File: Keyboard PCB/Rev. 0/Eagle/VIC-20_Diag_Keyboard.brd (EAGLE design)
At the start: 14 x 53 mm, 8 parts, among them J1 BL1-85AXX-20U

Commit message: Add files via upload
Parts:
- added U$10: (no value), Logo:VIC20_DIAG_SMALL
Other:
- board text added: "Keyboard Dongle Rev. 0"
- board text removed: "VIC-20 Diagnostic Keyboard Dongle Rev. 0"
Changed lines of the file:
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@@
 <?xml version="1.0" encoding="utf-8"?>
 <!DOCTYPE eagle SYSTEM "eagle.dtd">
-<eagle version="9.5.2">
+<eagle version="9.6.2">
 <drawing>
 <settings>
@@
 <wire x1="14" y1="0" x2="14" y2="53" width="0" layer="20"/>
 <wire x1="14" y1="53" x2="0" y2="53" width="0" layer="20"/>
-<text x="10.06625" y="39.6825" size="1.27" layer="21" rot="SR270">VIC-20 Diagnostic
-Keyboard Dongle Rev. 0</text>
+<text x="6.415" y="41.905" size="1.27" layer="21" rot="SR270">Keyboard Dongle Rev. 0</text>
 <wire x1="6.19125" y1="5.08" x2="8.5725" y2="5.08" width="0.1524" layer="21"/>
 <wire x1="8.5725" y1="5.08" x2="10.00125" y2="6.50875" width="0.1524" layer="21"/>
@@
 <text x="6.35" y="3.01625" size="1.778" layer="21" ratio="12" rot="SR270">1</text>
 <text x="6.19125" y="51.7525" size="1.778" layer="21" ratio="12" rot="SR270">20</text>
-<text x="8.73125" y="48.73625" size="1.27" layer="21" rot="SR270">!RESTORE</text>
+<text x="8.5725" y="50.4825" size="1.27" layer="21" rot="SR270">!RESTORE</text>
 <hole x="11.90625" y="49.8475" drill="2"/>
 <text x="1.905" y="44.29125" size="1.27" layer="22" rot="MR270">http://github.com/svenpetersen1965</text>
@@
 </element>
 <element name="U$8" library="Logo" package="SVEN_TAG" value="" x="9.525" y="39.52875" smashed="yes" rot="MR0"/>
+<element name="U$10" library="Logo" package="VIC20_DIAG_SMALL" value="" x="8.89" y="41.91" smashed="yes" rot="R270"/>
 </elements>
 <signals>

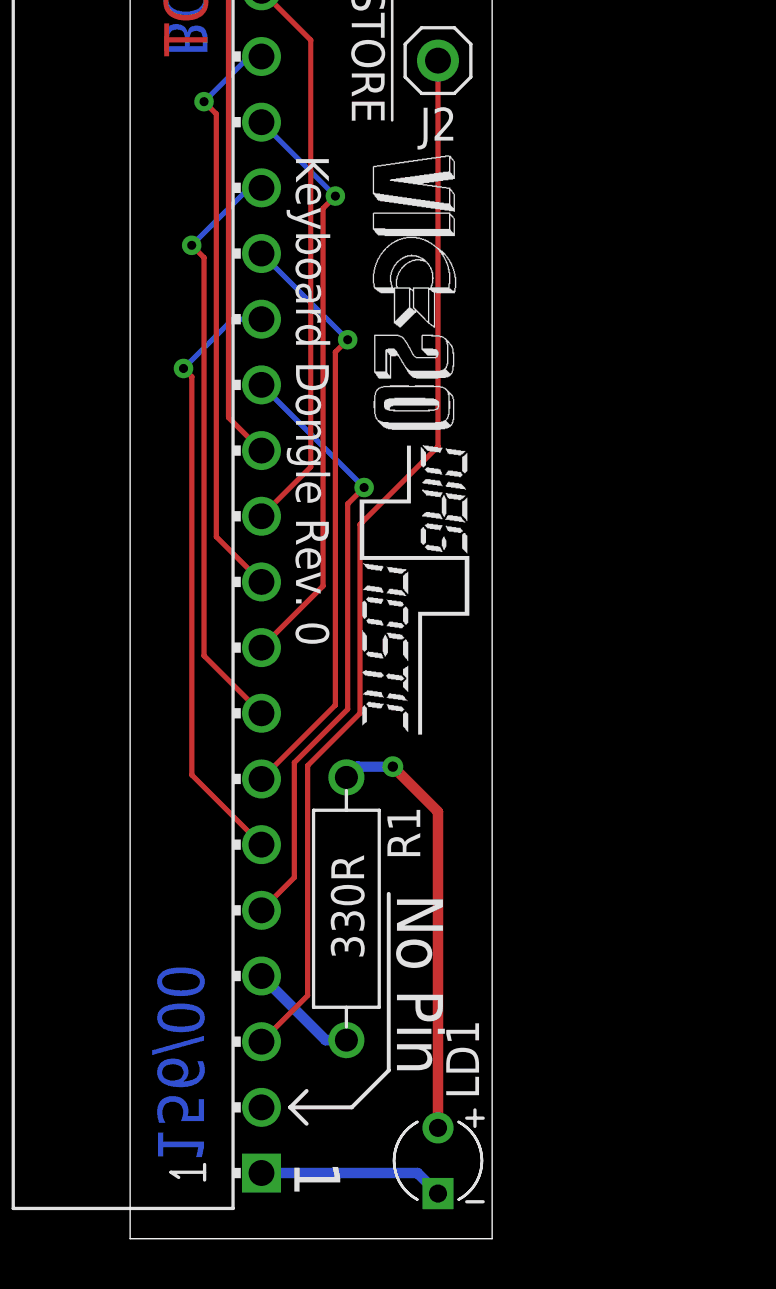
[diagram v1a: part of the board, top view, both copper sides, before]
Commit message: Silk Screen Update
Just a new logo
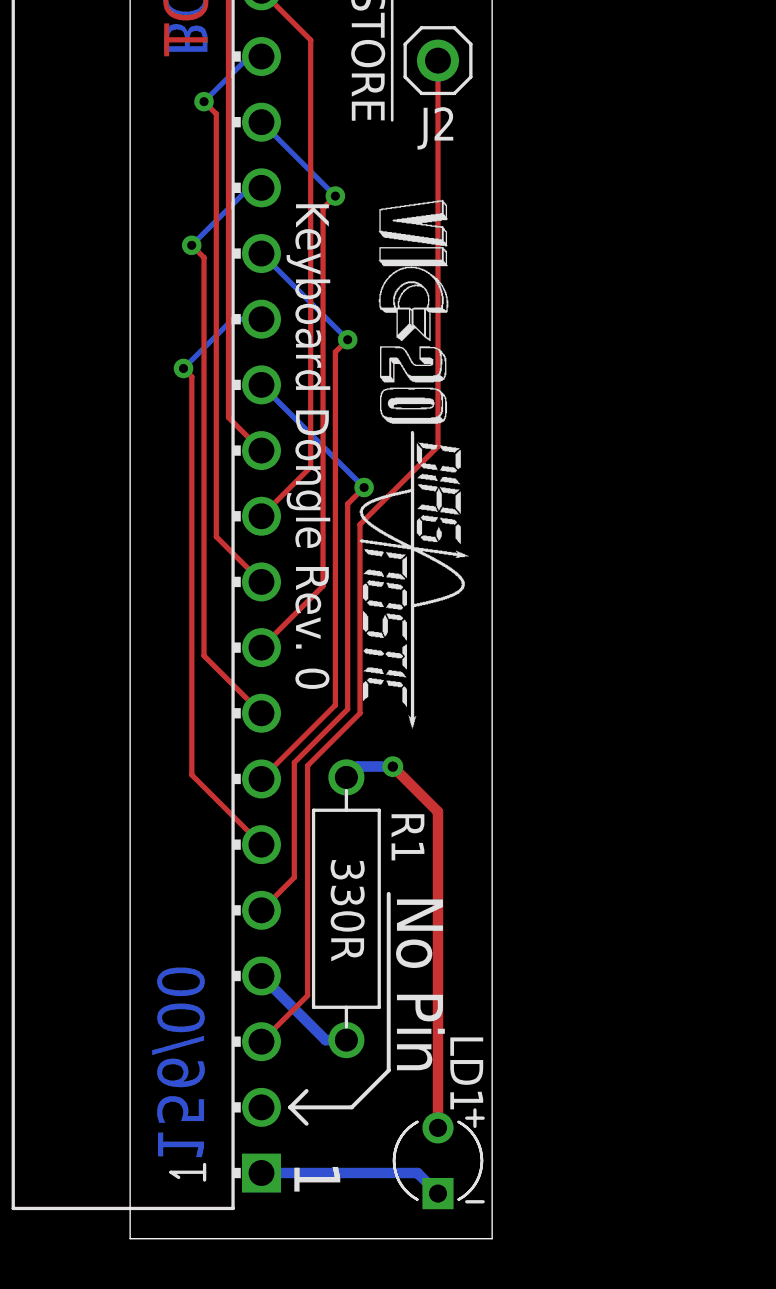
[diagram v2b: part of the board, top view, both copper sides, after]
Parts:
- moved U$10 1.75 mm to (8.89, 40.2)
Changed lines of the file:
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@@
 <layer number="45" name="Holes" color="7" fill="1" visible="no" active="yes"/>
 <layer number="46" name="Milling" color="3" fill="1" visible="no" active="yes"/>
-<layer number="47" name="Measures" color="7" fill="1" visible="no" active="yes"/>
+<layer number="47" name="Measures" color="7" fill="1" visible="yes" active="yes"/>
 <layer number="48" name="Document" color="5" fill="1" visible="yes" active="yes"/>
 <layer number="49" name="Reference" color="7" fill="1" visible="yes" active="yes"/>
@@
 <wire x1="14" y1="0" x2="14" y2="53" width="0" layer="20"/>
 <wire x1="14" y1="53" x2="0" y2="53" width="0" layer="20"/>
-<text x="6.415" y="41.905" size="1.27" layer="21" rot="SR270">Keyboard Dongle Rev. 0</text>
+<text x="6.415" y="40.15875" size="1.27" layer="21" rot="SR270">Keyboard Dongle Rev. 0</text>
 <wire x1="6.19125" y1="5.08" x2="8.5725" y2="5.08" width="0.1524" layer="21"/>
 <wire x1="8.5725" y1="5.08" x2="10.00125" y2="6.50875" width="0.1524" layer="21"/>
@@
 <hole x="11.90625" y="49.8475" drill="2"/>
 <text x="1.905" y="44.29125" size="1.27" layer="22" rot="MR270">http://github.com/svenpetersen1965</text>
-<text x="9.04875" y="10.795" size="1.27" layer="21" rot="R90">330R</text>
+<text x="7.77875" y="14.76375" size="1.27" layer="21" rot="SR270">330R</text>
 </plain>
 <attributes>
@@
 </element>
 <element name="LD1" library="LED" package="3MM" value="" x="11.90625" y="3.01625" smashed="yes" rot="R270">
-<attribute name="NAME" x="13.49375" y="5.3975" size="1.27" layer="25" ratio="10" rot="R90"/>
+<attribute name="NAME" x="12.3825" y="7.9375" size="1.27" layer="25" ratio="10" rot="SR270"/>
 <attribute name="VALUE" x="10.31875" y="1.11125" size="1.27" layer="27" ratio="10" rot="R270"/>
 </element>
 <element name="R1" library="DISCRETE" package="R-10" value="330R" x="8.36375" y="12.76" smashed="yes" rot="R270">
-<attribute name="NAME" x="9.95125" y="16.72875" size="1.27" layer="25" rot="R270"/>
-<attribute name="VALUE" x="7.72875" y="15.935" size="1.27" layer="27" rot="R270"/>
+<attribute name="NAME" x="10.11" y="16.57" size="1.27" layer="25" rot="SR270"/>
+<attribute name="VALUE" x="7.72875" y="14.665" size="1.27" layer="27" rot="SR270"/>
 </element>
 <element name="U$6" library="I-TEILE" package="2LAYER" value="" x="2.99375" y="45.73125" smashed="yes" rot="R90"/>
@@
 </element>
 <element name="U$8" library="Logo" package="SVEN_TAG" value="" x="9.525" y="39.52875" smashed="yes" rot="MR0"/>
-<element name="U$10" library="Logo" package="VIC20_DIAG_SMALL" value="" x="8.89" y="41.91" smashed="yes" rot="R270"/>
+<element name="U$10" library="Logo" package="VIC20_DIAG_SMALL" value="" x="8.89" y="40.16375" smashed="yes" rot="R270"/>
 </elements>
 <signals>
